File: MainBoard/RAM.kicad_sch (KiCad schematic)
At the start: 6 parts, among them IC5001 7028L20PFGI, U5009 ATF22V10C, U5010 CD74HC173PWR

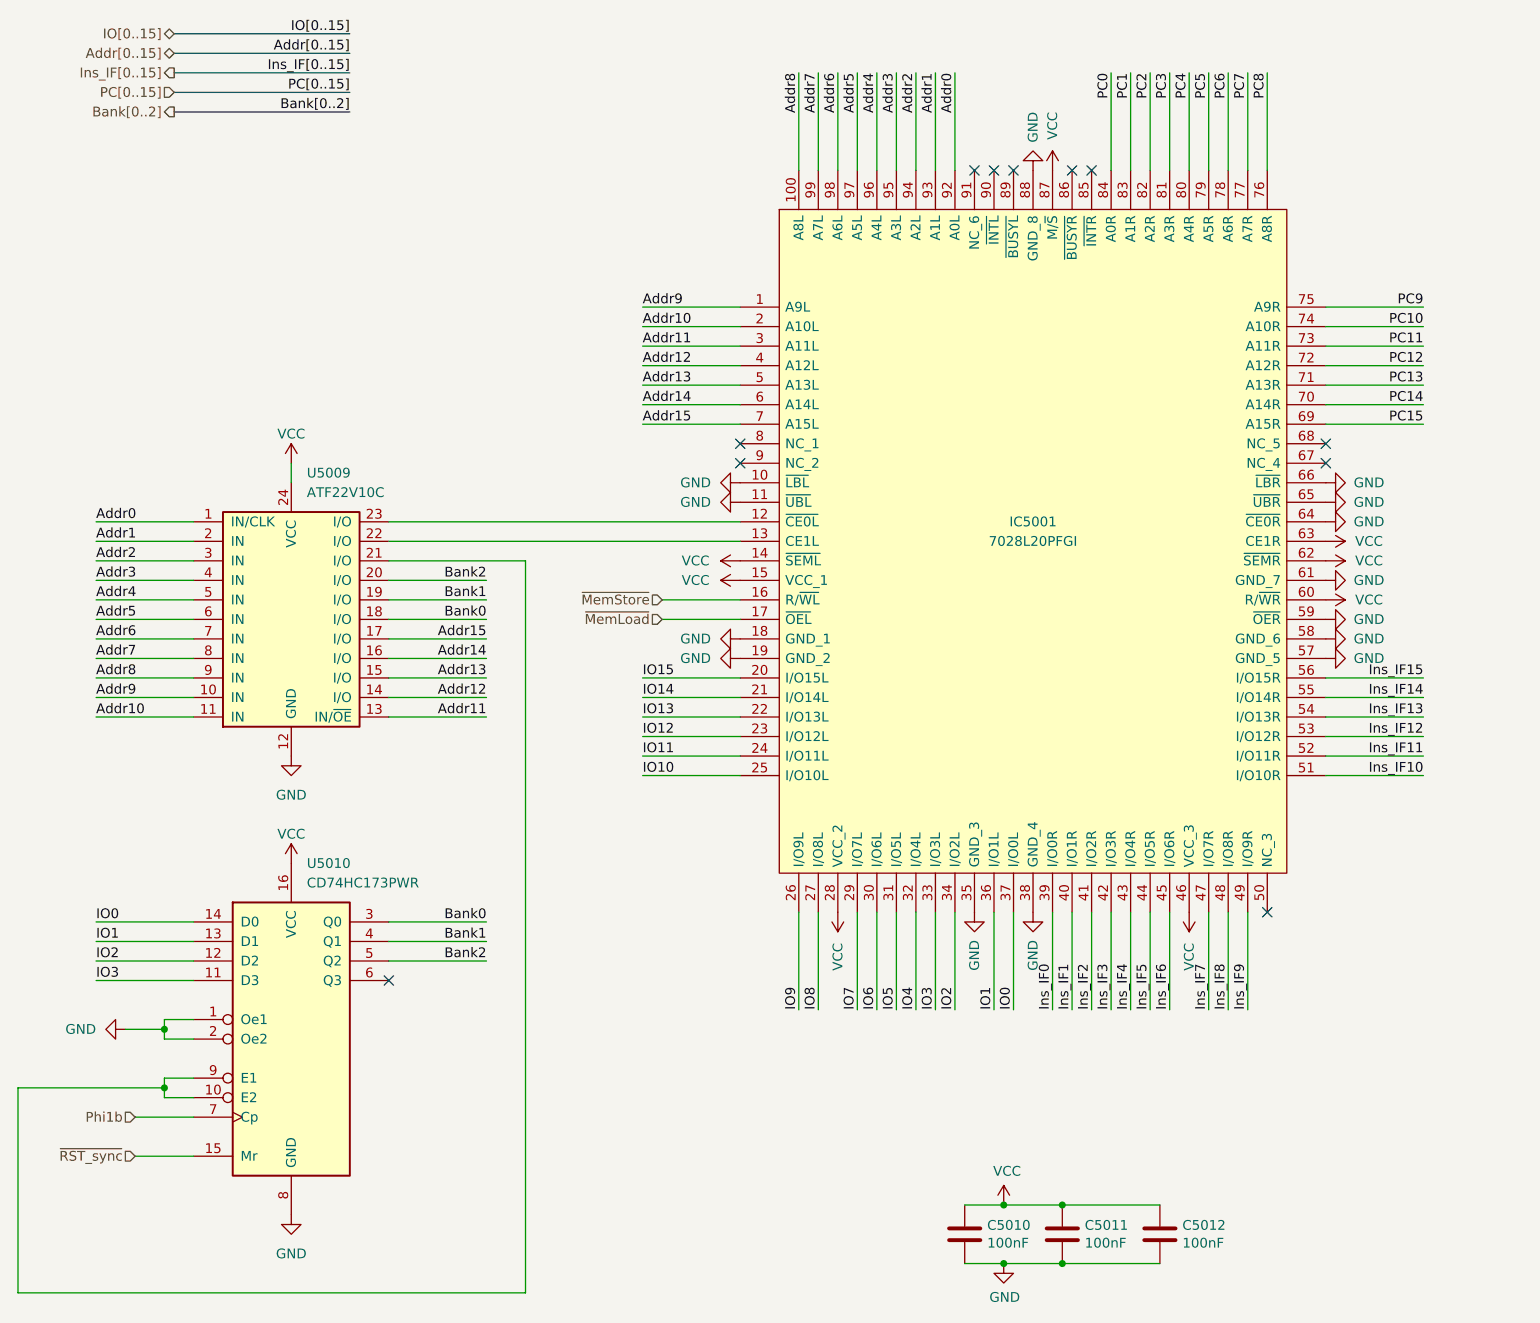
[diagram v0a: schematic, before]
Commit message: Place footprints on monlithic PCB
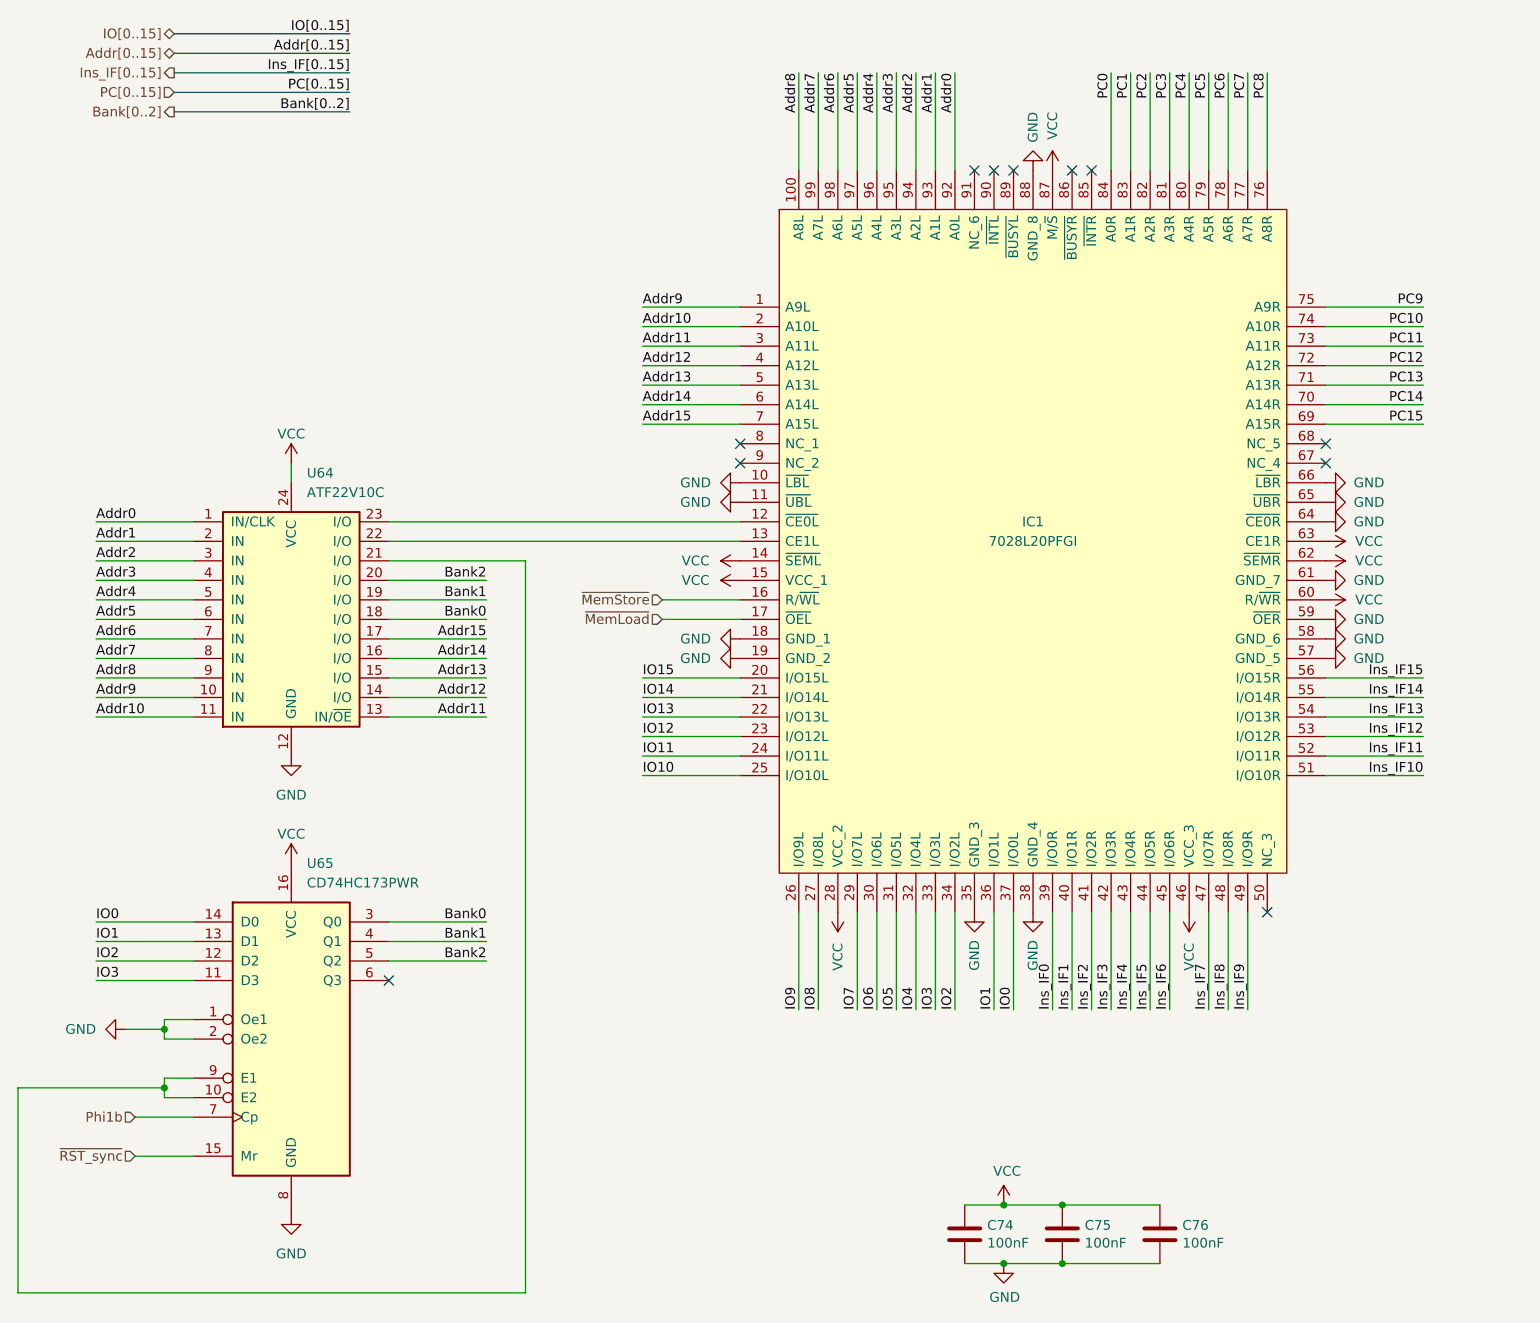
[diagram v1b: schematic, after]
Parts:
- renumbered C5010 to C74, C5011 to C75, C5012 to C76, IC5001 to IC1, U5009 to U64, U5010 to U65

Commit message: MainBoard: Add FLUSH_IF signal
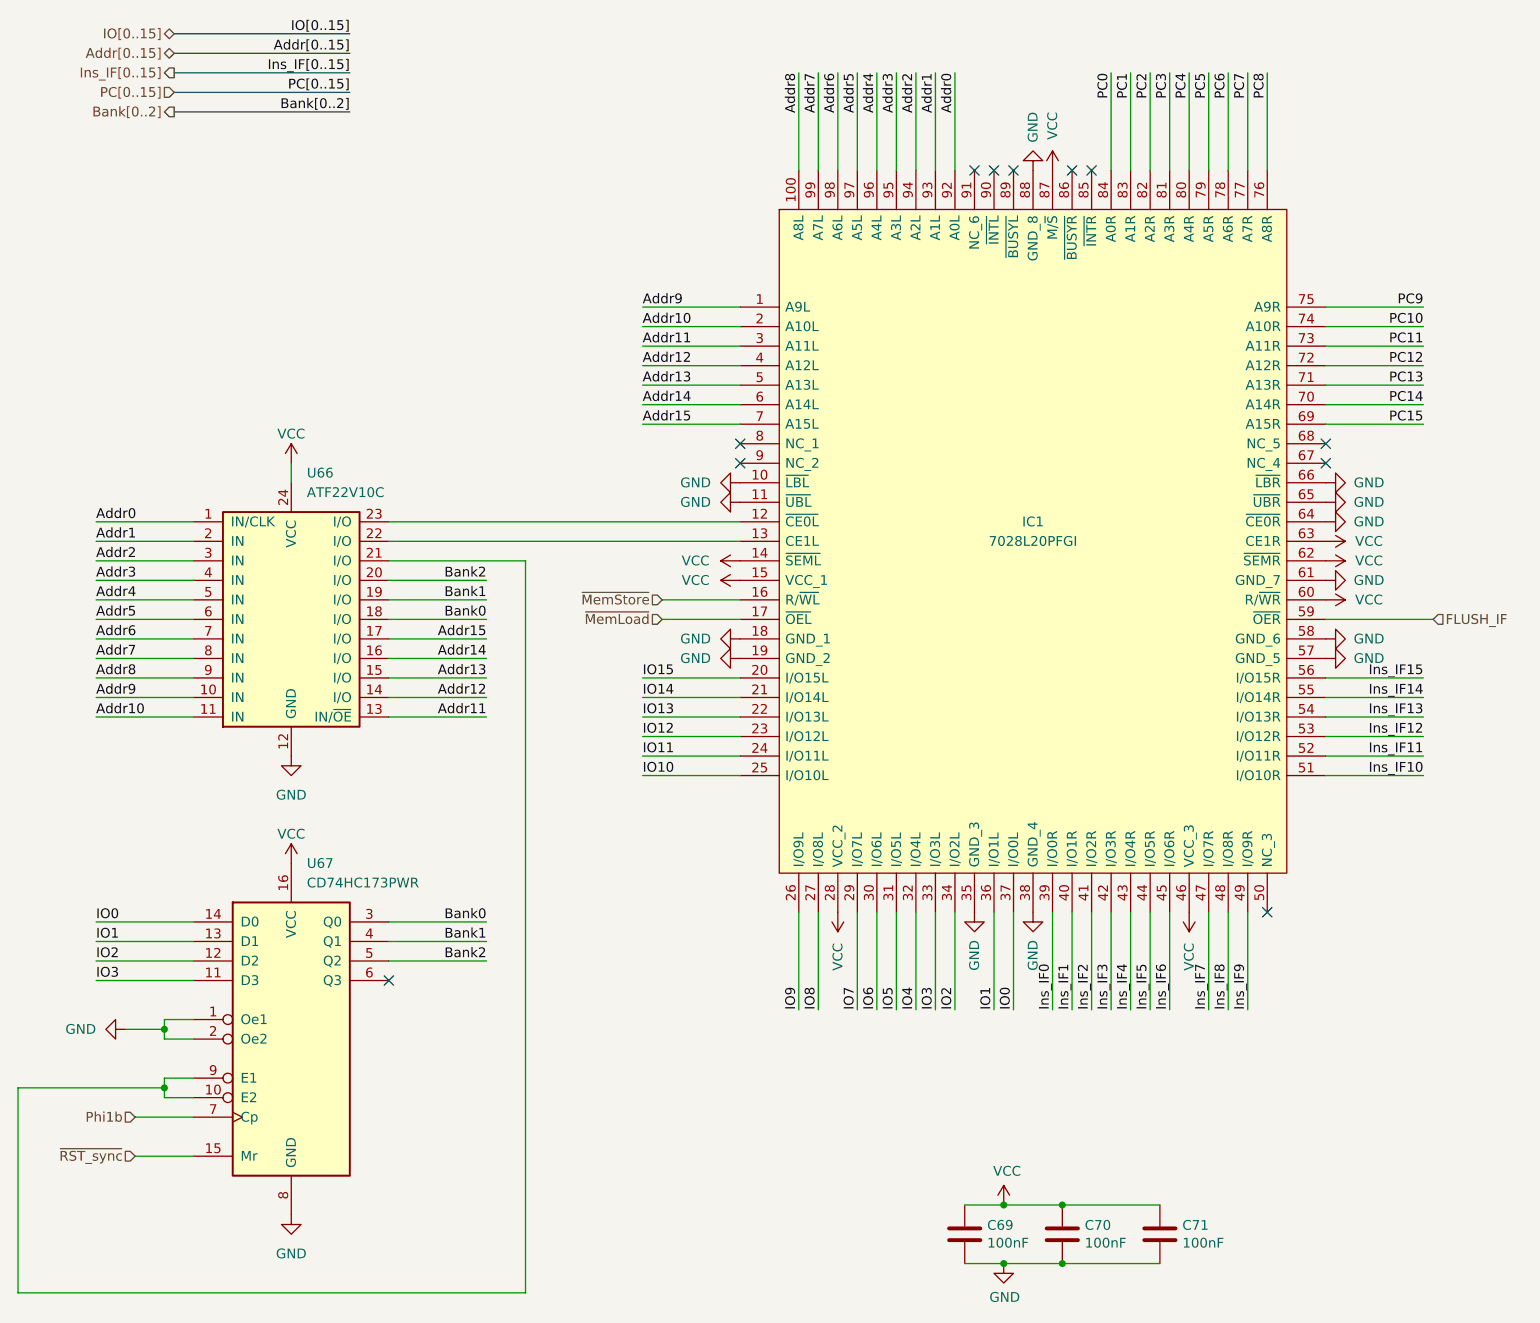
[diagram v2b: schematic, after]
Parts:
- renumbered C74 to C69, C75 to C70, C76 to C71, U64 to U66, U65 to U67
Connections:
- net GND: no longer IC1.59 (~{OER})
- new net FLUSH_IF: IC1.59 (~{OER})

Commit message: MainBoard: Fix power connector footprint
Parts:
- IC1: footprint Package_QFP:TQFP-100_14x14mm_P0.5mm -> QFP50P1600X1600X160-100N
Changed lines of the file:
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@@
     (property "Reference" "IC1" (id 0) (at 149.86 93.98 0))
     (property "Value" "7028L20PFGI" (id 1) (at 149.86 96.52 0))
-    (property "Footprint" "Package_QFP:TQFP-100_14x14mm_P0.5mm" (id 2) (at 184.15 53.34 0)
+    (property "Footprint" "QFP50P1600X1600X160-100N" (id 2) (at 184.15 53.34 0)
       (effects (font (size 1.27 1.27)) (justify left) hide)
     )
@@
       (effects (font (size 1.27 1.27)) hide)
     )
-    (property "Datasheet" "http://www.ti.com/general/docs/suppproductinfo.tsp?distId=26&gotoUrl=http%3A%2F%2Fwww.ti.com%2Flit%2Fgpn%2Fcd74hc173" (id 3) (at 53.34 161.29 0)
-      (effects (font (size 1.27 1.27)) hide)
-    )
+    (property "Datasheet" "http://www.ti.com/lit/gpn/sn74LS173" (id 3) (at 53.34 161.29 0)
+      (effects (font (size 1.27 1.27)) hide)
+    )

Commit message: MainBoard: fix the footprint on the 7028 and 16374
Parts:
- IC1: footprint QFP50P1600X1600X160-100N -> Package_QFP:TQFP-100_14x14mm_P0.5mm
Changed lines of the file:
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@@
     (property "Reference" "IC1" (id 0) (at 149.86 93.98 0))
     (property "Value" "7028L20PFGI" (id 1) (at 149.86 96.52 0))
-    (property "Footprint" "QFP50P1600X1600X160-100N" (id 2) (at 184.15 53.34 0)
+    (property "Footprint" "Package_QFP:TQFP-100_14x14mm_P0.5mm" (id 2) (at 184.15 53.34 0)
       (effects (font (size 1.27 1.27)) (justify left) hide)
     )

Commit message: MainBoard: route the monolithic main board (Rev C)
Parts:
- IC1: value 7028L20PFGI -> (none)
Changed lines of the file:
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@@
-    (stroke (width 0) (type default) (color 0 0 0 0))
-  )
-  (wire (pts (xy 187.96 106.68) (xy 201.93 106.68))
     (stroke (width 0) (type default) (color 0 0 0 0))
   )
@@
   )
   (wire (pts (xy 153.67 182.88) (xy 166.37 182.88))
+    (stroke (width 0) (type default) (color 0 0 0 0))
+  )
+  (wire (pts (xy 198.12 106.68) (xy 187.96 106.68))
     (stroke (width 0) (type default) (color 0 0 0 0))
   )
@@
     (effects (font (size 1.27 1.27)) (justify right))
   )
+  (hierarchical_label "FLUSH_IF" (shape input) (at 198.12 106.68 0)
+    (effects (font (size 1.27 1.27)) (justify left))
+  )
   (hierarchical_label "Addr[0..15]" (shape tri_state) (at 38.1 33.02 180)
     (effects (font (size 1.27 1.27)) (justify right))
@@
   (hierarchical_label "~{MemLoad}" (shape input) (at 101.6 106.68 180)
     (effects (font (size 1.27 1.27)) (justify right))
-  )
-  (hierarchical_label "FLUSH_IF" (shape input) (at 201.93 106.68 0)
-    (effects (font (size 1.27 1.27)) (justify left))
   )
   (symbol (lib_id "power:GND") (at 149.86 144.78 0) (unit 1)
@@
     (in_bom yes) (on_board yes)
     (property "Reference" "IC1" (id 0) (at 149.86 93.98 0))
-    (property "Value" "7028L20PFGI" (id 1) (at 149.86 96.52 0))
+    (property "Value" "" (id 1) (at 149.86 96.52 0))
     (property "Footprint" "Package_QFP:TQFP-100_14x14mm_P0.5mm" (id 2) (at 184.15 53.34 0)
       (effects (font (size 1.27 1.27)) (justify left) hide)
@@
       (effects (font (size 1.27 1.27)) hide)
     )
-    (property "Datasheet" "http://www.ti.com/lit/gpn/sn74LS173" (id 3) (at 53.34 161.29 0)
-      (effects (font (size 1.27 1.27)) hide)
-    )
+    (property "Datasheet" "http://www.ti.com/general/docs/suppproductinfo.tsp?distId=26&gotoUrl=http%3A%2F%2Fwww.ti.com%2Flit%2Fgpn%2Fcd74hc173" (id 3) (at 53.34 161.29 0)
+      (effects (font (size 1.27 1.27)) hide)
+    )

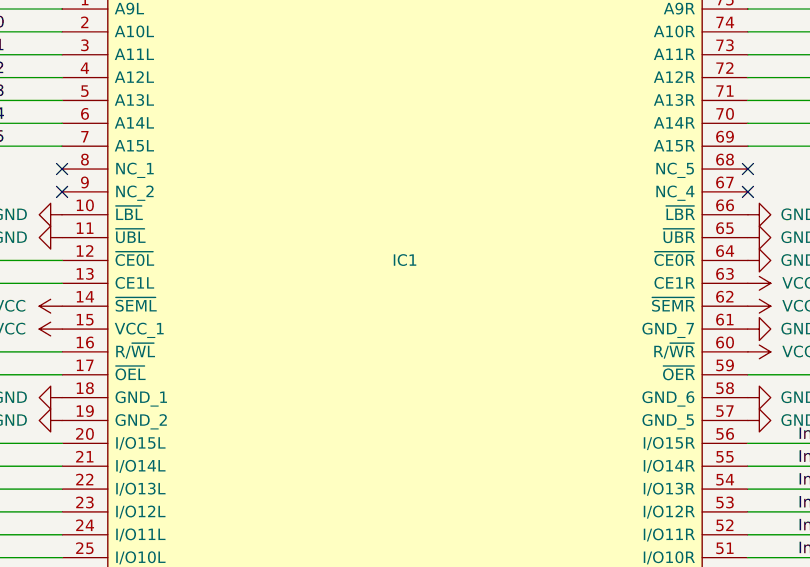
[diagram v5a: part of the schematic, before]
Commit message: MainBoard, ControlModule: route reset signal to HazardControl
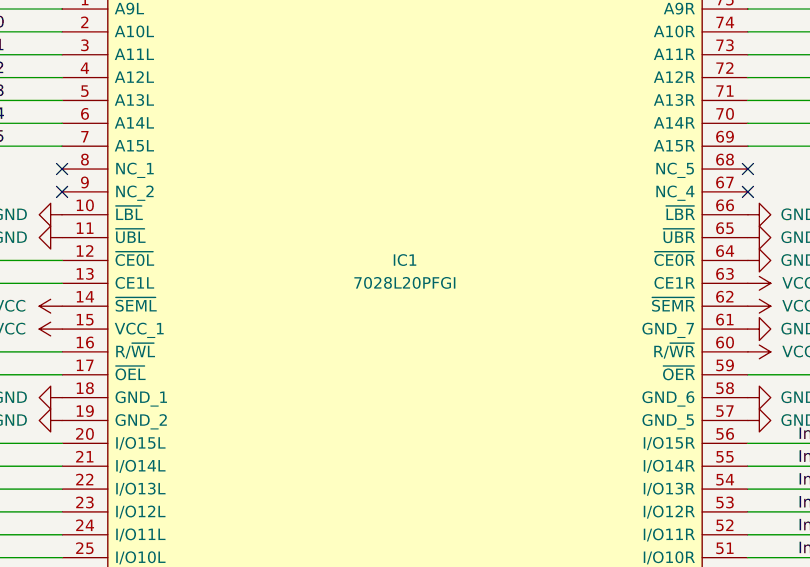
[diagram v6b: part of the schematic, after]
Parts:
- IC1: value (none) -> 7028L20PFGI
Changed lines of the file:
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@@
     (in_bom yes) (on_board yes)
     (property "Reference" "IC1" (id 0) (at 149.86 93.98 0))
-    (property "Value" "" (id 1) (at 149.86 96.52 0))
+    (property "Value" "7028L20PFGI" (id 1) (at 149.86 96.52 0))
     (property "Footprint" "Package_QFP:TQFP-100_14x14mm_P0.5mm" (id 2) (at 184.15 53.34 0)
       (effects (font (size 1.27 1.27)) (justify left) hide)
